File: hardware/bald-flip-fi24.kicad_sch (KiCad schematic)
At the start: 35 parts, among them J1 Flipper Header, J2 USB4105-GF-A, J3 Flipper Board Outline (Large), Q1 DMN2058U, Q2 DMN2058U, SW1 5V Src, SW1 esp PWR, SW1 nRF PWR, SW3 Boot, SW4 Reset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

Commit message: moved nrf24 to front, I like it better
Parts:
- added D5: nRF, LED_SMD:LED_0805_2012Metric_Pad1.15x1.40mm_HandSolder, symbol My Library:D_1206
- added R12: 4k7, Resistor_SMD:R_0805_2012Metric, symbol My Library:R_0805
- D1: footprint LED_SMD:LED_1206_3216Metric -> LED_SMD:LED_0805_2012Metric_Pad1.15x1.40mm_HandSolder
- D2: value 3v3 -> ESP; footprint LED_SMD:LED_1206_3216Metric -> LED_SMD:LED_0805_2012Metric_Pad1.15x1.40mm_HandSolder
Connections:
- net +3V3: no longer R2.1, R4.1, R5.1
- net GND: now also D5.1 (K)
- net esp_VCC: now also R2.1, R4.1, R5.1
- net nRF_VCC: now also R12.1
- new net: D5.2 (A), R12.2
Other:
- moved on the sheet: D1, D2, J3, R1, R2, R4, SW3

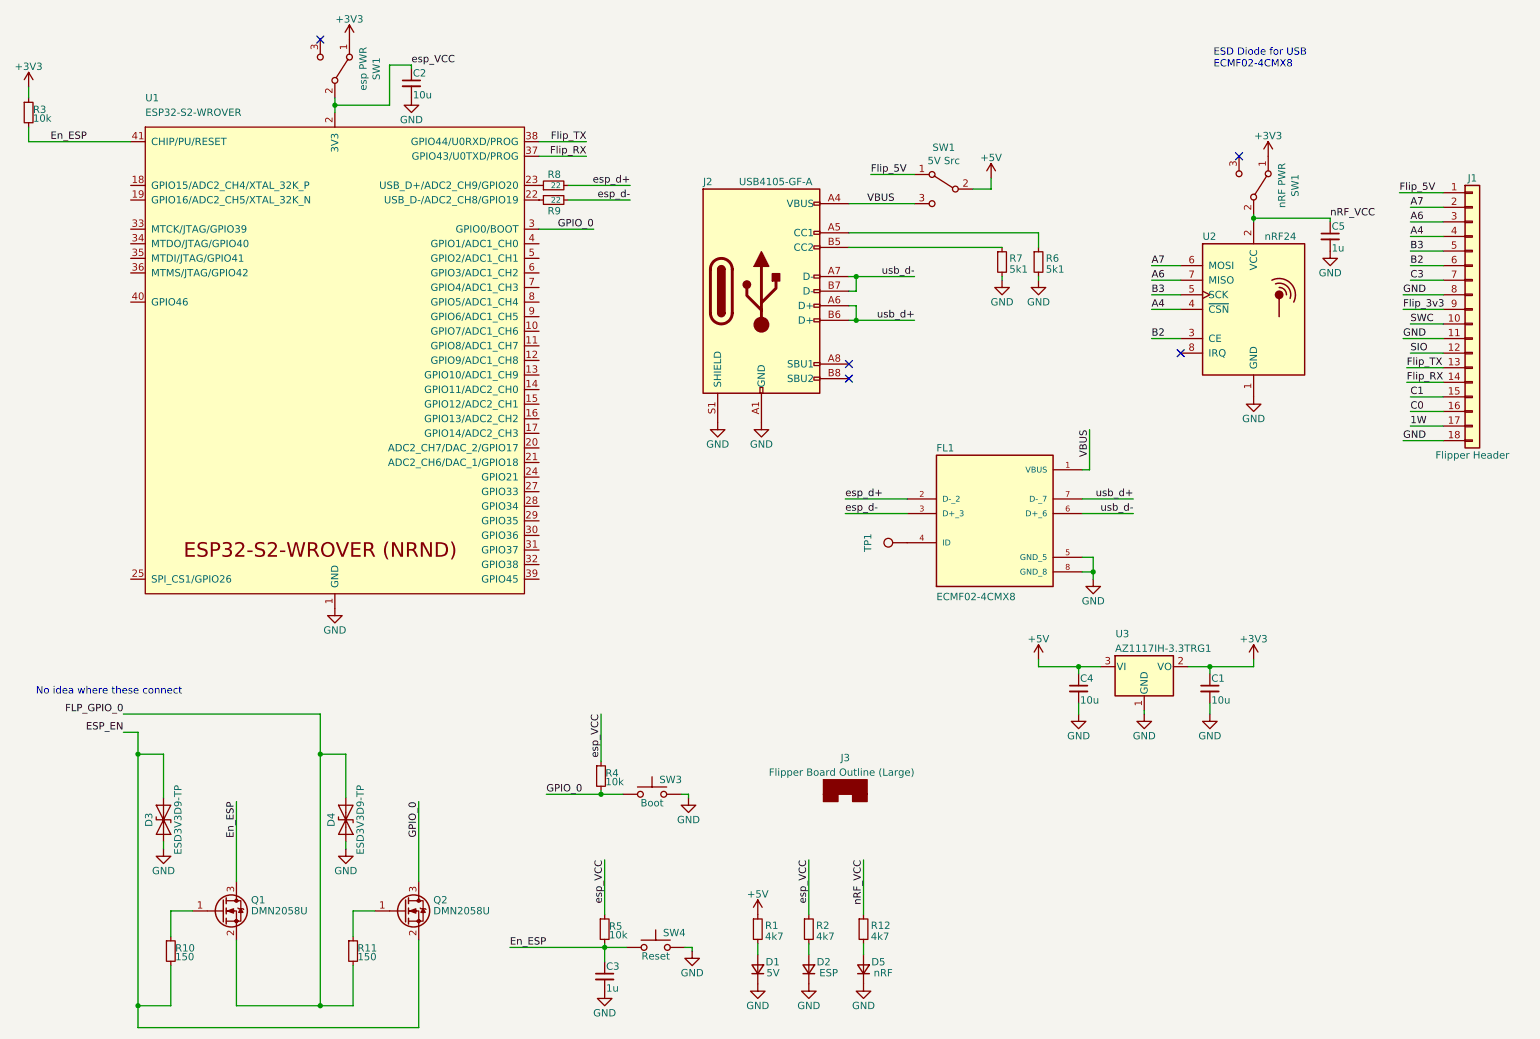
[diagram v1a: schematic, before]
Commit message: re-worked SPi signals, need to consider if firmware can handle moving CS. Cleaned up some silk (for now).
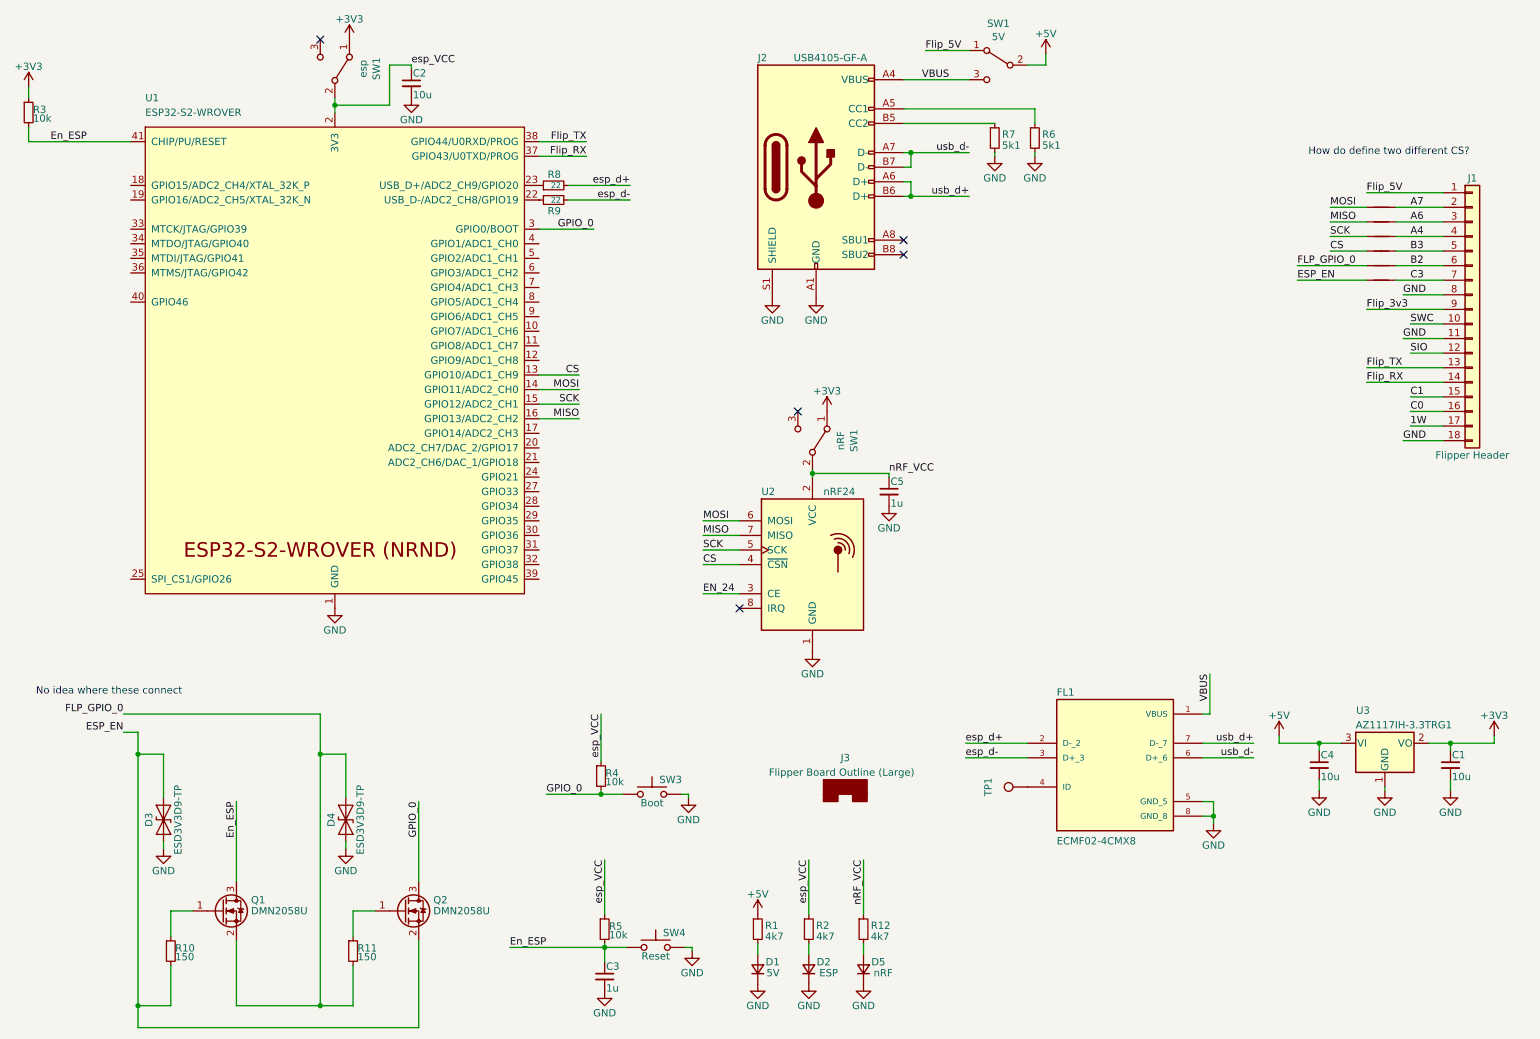
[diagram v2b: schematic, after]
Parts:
- added NT1, NT2, NT3, NT4, NT5, NT6: NetTie_2, NetTie:NetTie-2_SMD_Pad0.5mm, symbol Device:NetTie_2
- SW1: value nRF PWR -> nRF
- SW1: value esp PWR -> esp
- SW1: value 5V Src -> 5V
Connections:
- net A4: now also NT5.2; no longer U2.4 (~{CSN})
- net A6: now also NT4.2; no longer U2.7 (MISO)
- net A7: now also NT3.2; no longer U2.6 (MOSI)
- net B2: now also NT1.2; no longer U2.3 (CE)
- net B3: now also NT6.2; no longer U2.5 (SCK)
- net C3: now also NT2.2
- net ESP_EN: now also NT2.1
- net FLP_GPIO_0: now also NT1.1
- net CS: now reaches U1.13 (GPIO10/ADC1_CH9)
- net CS: now also U2.4 (~{CSN}), NT6.1
- net MOSI: now reaches U1.14 (GPIO11/ADC2_CH0)
- net MOSI: now also U2.6 (MOSI), NT3.1
- net SCK: now reaches U1.15 (GPIO12/ADC2_CH1)
- net SCK: now also U2.5 (SCK), NT5.1
- net MISO: now reaches U1.16 (GPIO13/ADC2_CH2)
- net MISO: now also U2.7 (MISO), NT4.1
- new net EN_24: U2.3 (CE)
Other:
- note added: "How do define two different CS?"
- note removed: "ESD Diode for USB ECMF02-4CMX8"
- moved on the sheet: C1, C4, C5, FL1, J2, R6, R7, SW1, TP1, U2, U3

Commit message: added RGB and test points
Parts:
- removed NT1, NT2, NT3, NT4, NT5, NT6: NetTie_2, NetTie:NetTie-2_SMD_Pad0.5mm, symbol Device:NetTie_2
- added D6: LTST-C19HE1WT, LED_SMD:LED_LiteOn_LTST-C19HE1WT, symbol Device:LED_RGBA
- added JP1: Jumper_2_Bridged, Jumper:SolderJumper-2_P1.3mm_Bridged_RoundedPad1.0x1.5mm, symbol Jumper:Jumper_2_Bridged
- added R13, R14: 1k, Resistor_SMD:R_0805_2012Metric, symbol My Library:R_0805
- added R15: 5.1k, Resistor_SMD:R_0805_2012Metric, symbol My Library:R_0805
- added TP10, TP11, TP12, TP2, TP3, TP4, TP5, TP6, TP7, TP8, TP9: TestPoint_Harwin, My Libraries:Harwin-S1751-46-Test-Point, symbol My Library:TestPoint_Harwin
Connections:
- net CS is gone; now on net B3: U1.13 (GPIO10/ADC1_CH9), U2.4 (~{CSN})
- net ESP_EN is gone; now on net C3: D3.2 (A2), Q2.2 (S), R10.2
- net FLP_GPIO_0 is gone; now on net B2: D4.2 (A2), Q1.2 (S), R11.2
- net MISO is gone; now on net A6: U1.16 (GPIO13/ADC2_CH2), U2.7 (MISO)
- net MOSI is gone; now on net A7: U1.14 (GPIO11/ADC2_CH0), U2.6 (MOSI)
- net SCK is gone; now on net A4: U1.15 (GPIO12/ADC2_CH1), U2.5 (SCK)
- net +3V3: now also SW1.3 (C), SW1.3 (C), TP11.1; no longer SW1.1 (A), SW1.1 (A)
- net +5V: now also TP8.1
- net A4: now also TP6.1
- net A6: now also TP7.1
- net A7: now also TP5.1
- net B3: now also TP12.1, TP4.1
- net Flip_5V: now also SW1.3 (C), TP9.1; no longer SW1.1 (A)
- net GPIO_0: now also TP2.1
- net VBUS: now also SW1.1 (A); no longer SW1.3 (C)
- net nRF_VCC: now also JP1.2 (B), TP10.1
- net I2C_PU: now reaches U1.6 (GPIO3/ADC1_CH2)
- net I2C_PU: now also TP3.1
- net Blu: now reaches U1.7 (GPIO4/ADC1_CH3)
- net Blu: now also R13.2
- net Grn: now reaches U1.8 (GPIO5/ADC1_CH4)
- net Grn: now also R14.2
- net Red: now reaches U1.9 (GPIO6/ADC1_CH5)
- net Red: now also R15.2
- new net: D6.1 (RK), R15.1
- new net: D6.2 (GK), R14.1
- new net: D6.3 (BK), R13.1
- new net: D6.4 (A), JP1.1 (A)
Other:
- moved on the sheet: C1, C4, FL1, J3, SW1, TP1, U3
